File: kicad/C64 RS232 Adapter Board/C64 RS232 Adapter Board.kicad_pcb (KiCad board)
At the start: 2 copper layers, 59.6 x 53.1 mm, 29 parts, among them J1 RS232_HDR, J2 DB25_RS232, J3 C64_USER_PORT, J4 User Port Breakout, SW1 RESET, U1 MAX3241ECAI+T

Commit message: rounded the corner yo
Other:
- board size 59.6 x 53.1 mm -> 60 x 54 mm
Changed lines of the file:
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@@
   (general
     (thickness 1.6)
-    (drawings 37)
+    (drawings 41)
     (tracks 306)
     (zones 0)
@@
     (46 B.CrtYd user)
     (47 F.CrtYd user)
-    (48 B.Fab user hide)
-    (49 F.Fab user hide)
+    (48 B.Fab user)
+    (49 F.Fab user)
   )
   (setup
@@
     (pad_to_mask_clearance 0.05)
     (aux_axis_origin 0 0)
-    (visible_elements 7FFFEFFF)
+    (visible_elements 7FFFF7FF)
     (pcbplotparams
       (layerselection 0x010fc_ffffffff)
@@
     (pad 1 np_thru_hole circle (at 0 0) (size 2.5 2.5) (drill 2.5) (layers *.Cu *.Mask))
   )
-  (gr_line (start 44.196 53.467) (end 103.759 53.467) (layer Edge.Cuts) (width 0.05))
-  (gr_line (start 44.196 106.553) (end 44.196 53.467) (layer Edge.Cuts) (width 0.05))
-  (gr_line (start 103.759 106.553) (end 44.196 106.553) (layer Edge.Cuts) (width 0.05))
-  (gr_line (start 103.759 53.467) (end 103.759 106.553) (layer Edge.Cuts) (width 0.05))
+  (gr_line (start 47 53) (end 101 53) (layer Edge.Cuts) (width 0.05))
+  (gr_line (start 44 104) (end 44 56) (layer Edge.Cuts) (width 0.05))
+  (gr_line (start 101 107) (end 47 107) (layer Edge.Cuts) (width 0.05))
+  (gr_line (start 104 56) (end 104 104) (layer Edge.Cuts) (width 0.05))
+  (gr_arc (start 47 56) (end 47 53) (angle -90) (layer Edge.Cuts) (width 0.05))
+  (gr_arc (start 47 104) (end 44 104) (angle -90) (layer Edge.Cuts) (width 0.05))
+  (gr_arc (start 101 56) (end 104 56) (angle -90) (layer Edge.Cuts) (width 0.05))
+  (gr_arc (start 101 104) (end 101 107) (angle -90) (layer Edge.Cuts) (width 0.05))
   (gr_text PWR (at 89.027 105.41) (layer F.SilkS)
     (effects (font (size 0.5 0.5) (thickness 0.1)))

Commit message: add some labels or something and stuff
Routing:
- net GND: track 5.25 -> 14.3 mm, vias 16 -> 37
- net /DCD_232: track 22.0 -> 18.5 mm, vias 0 -> 2
- net /RI_232: track 25.9 -> 23.9 mm
- net /DTR_232: track 14.4 -> 12.6 mm
- net /RTS_TTL: track 24.0 -> 22.5 mm
- net /DCD_TTL: track 10.1 -> 8.87 mm
- net /TXD_TTL: track 25.4 -> 26.3 mm
- net /RI_TTL: track 13.4 -> 12.7 mm
- net /DTR_TTL: track 24.8 -> 24.3 mm
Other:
- board text added: "5V"
- board text added: "CTS"
- board text added: "DCD"
- board text added: "DSR"
- board text added: "DTR"
- board text added: "RI"
- board text added: "RTS"
- board text added: "RXD"
- board text added: "TXD"

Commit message: let's do that!
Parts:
- added REF**: Bald_Slot_2mm_X_10mm, My Libraries:Bald_Slot_2mm_X_10mm, F.Cu at (72.7, 100.4)
- added REF**: Bald_Slot_2mm_X_10mm, My Libraries:Bald_Slot_2mm_X_10mm, F.Cu at (72.7, 86.9)
- added REF**: Bald_Slot_2mm_X_10mm, My Libraries:Bald_Slot_2mm_X_10mm, F.Cu at (72.7, 73.6)
- added REF**: Bald_Slot_2mm_X_10mm, My Libraries:Bald_Slot_2mm_X_10mm, F.Cu at (72.7, 59.7)
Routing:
- net GND: vias 37 -> 40
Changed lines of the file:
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@@
     (thickness 1.6)
     (drawings 115)
-    (tracks 354)
+    (tracks 357)
     (zones 0)
-    (modules 29)
+    (modules 33)
     (nets 65)
   )
@@
     (via_min_size 0.4)
     (via_min_drill 0.3)
+    (user_via 3 2)
     (uvia_size 0.3)
     (uvia_drill 0.1)
@@
     (add_net "Net-(U1-Pad20)")
     (add_net "Net-(U1-Pad21)")
+  )
+  (module "My Libraries:Bald_Slot_2mm_X_10mm" (layer F.Cu)
+    (at 72.7176 100.4062)
+    (fp_text reference REF** (at 0 0.5) (layer F.SilkS)
+      (effects (font (size 1 1) (thickness 0.15)))
+    )
+    (fp_text value Bald_Slot_2mm_X_10mm (at 0 -0.5) (layer F.Fab)
+      (effects (font (size 1 1) (thickness 0.15)))
+    )
+    (pad 1 thru_hole oval (at 0.0254 -0.0254) (size 4 12) (drill oval 2 10) (layers *.Cu *.Mask))
+  )
+  (module "My Libraries:Bald_Slot_2mm_X_10mm" (layer F.Cu)
+    (at 72.7176 86.8934)
+    (fp_text reference REF** (at 0 0.5) (layer F.SilkS)
+      (effects (font (size 1 1) (thickness 0.15)))
+    )
+    (fp_text value Bald_Slot_2mm_X_10mm (at 0 -0.5) (layer F.Fab)
+      (effects (font (size 1 1) (thickness 0.15)))
+    )
+    (pad 1 thru_hole oval (at 0.0254 -0.0254) (size 4 12) (drill oval 2 10) (layers *.Cu *.Mask))
+  )
+  (module "My Libraries:Bald_Slot_2mm_X_10mm" (layer F.Cu)
+    (at 72.7176 73.5584)
+    (fp_text reference REF** (at 0 0.5) (layer F.SilkS)
+      (effects (font (size 1 1) (thickness 0.15)))
+    )
+    (fp_text value Bald_Slot_2mm_X_10mm (at 0 -0.5) (layer F.Fab)
+      (effects (font (size 1 1) (thickness 0.15)))
+    )
+    (pad 1 thru_hole oval (at 0.0254 -0.0254) (size 4 12) (drill oval 2 10) (layers *.Cu *.Mask))
+  )
+  (module "My Libraries:Bald_Slot_2mm_X_10mm" (layer F.Cu)
+    (at 72.7176 59.7408)
+    (fp_text reference REF** (at 0 0.5) (layer F.SilkS)
+      (effects (font (size 1 1) (thickness 0.15)))
+    )
+    (fp_text value Bald_Slot_2mm_X_10mm (at 0 -0.5) (layer F.Fab)
+      (effects (font (size 1 1) (thickness 0.15)))
+    )
+    (pad 1 thru_hole oval (at 0.0254 -0.0254) (size 4 12) (drill oval 2 10) (layers *.Cu *.Mask))
   )
   (module Package_SO:SSOP-28_5.3x10.2mm_P0.65mm (layer F.Cu)
@@
   (segment (start 98.933 84.963) (end 98.933 81.4832) (width 0.254) (layer B.Cu) (net 6))
   (via (at 98.933 84.963) (size 0.8) (drill 0.4) (layers F.Cu B.Cu) (net 6))
+  (via (at 71.0946 66.675) (size 0.8) (drill 0.4) (layers F.Cu B.Cu) (net 6))
+  (via (at 72.771 66.675) (size 0.8) (drill 0.4) (layers F.Cu B.Cu) (net 6))
+  (via (at 74.2696 66.675) (size 0.8) (drill 0.4) (layers F.Cu B.Cu) (net 6))
   (segment (start 93.894039 91.724303) (end 94.938401 91.724303) (width 0.254) (layer F.Cu) (net 7))
   (segment (start 93.2307 92.387642) (end 93.894039 91.724303) (width 0.254) (layer F.Cu) (net 7))

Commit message: Final Board (maybe?)
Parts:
- removed the REF** at (72.7, 100.4)
- removed the REF** at (72.7, 86.9)
- removed the REF** at (72.7, 73.6)
- removed the REF** at (72.7, 59.7)
- added REF**: 25mil_Hole, My Libraries:25mil_Hole, F.Cu at (71.5, 80.7)
- added e: 25mil_Hole, My Libraries:25mil_Hole, F.Cu at (74.4, 80.7)
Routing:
- net GND: vias 40 -> 37
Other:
- outline, holes or cut-outs redrawn
- board text added: "C64-User Breakout rev1"
- board text added: "RS-232 Breakout rev1"
- board text added: "james@baldengineer.com Hi Chat! You look nice today!"
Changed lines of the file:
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@@
   (general
     (thickness 1.6)
-    (drawings 115)
-    (tracks 357)
+    (drawings 126)
+    (tracks 354)
     (zones 0)
-    (modules 33)
+    (modules 31)
     (nets 65)
   )
   (page A4)
   (layers
-    (0 F.Cu signal)
-    (31 B.Cu signal)
+    (0 F.Cu signal hide)
+    (31 B.Cu signal hide)
     (32 B.Adhes user)
-    (33 F.Adhes user)
+    (33 F.Adhes user hide)
     (34 B.Paste user)
     (35 F.Paste user)
@@
     (add_net "Net-(U1-Pad21)")
   )
-  (module "My Libraries:Bald_Slot_2mm_X_10mm" (layer F.Cu)
-    (at 72.7176 100.4062)
-    (fp_text reference REF** (at 0 0.5) (layer F.SilkS)
-      (effects (font (size 1 1) (thickness 0.15)))
-    )
-    (fp_text value Bald_Slot_2mm_X_10mm (at 0 -0.5) (layer F.Fab)
-      (effects (font (size 1 1) (thickness 0.15)))
-    )
-    (pad 1 thru_hole oval (at 0.0254 -0.0254) (size 4 12) (drill oval 2 10) (layers *.Cu *.Mask))
-  )
-  (module "My Libraries:Bald_Slot_2mm_X_10mm" (layer F.Cu)
-    (at 72.7176 86.8934)
-    (fp_text reference REF** (at 0 0.5) (layer F.SilkS)
-      (effects (font (size 1 1) (thickness 0.15)))
-    )
-    (fp_text value Bald_Slot_2mm_X_10mm (at 0 -0.5) (layer F.Fab)
-      (effects (font (size 1 1) (thickness 0.15)))
-    )
-    (pad 1 thru_hole oval (at 0.0254 -0.0254) (size 4 12) (drill oval 2 10) (layers *.Cu *.Mask))
-  )
-  (module "My Libraries:Bald_Slot_2mm_X_10mm" (layer F.Cu)
-    (at 72.7176 73.5584)
-    (fp_text reference REF** (at 0 0.5) (layer F.SilkS)
-      (effects (font (size 1 1) (thickness 0.15)))
-    )
-    (fp_text value Bald_Slot_2mm_X_10mm (at 0 -0.5) (layer F.Fab)
-      (effects (font (size 1 1) (thickness 0.15)))
-    )
-    (pad 1 thru_hole oval (at 0.0254 -0.0254) (size 4 12) (drill oval 2 10) (layers *.Cu *.Mask))
-  )
-  (module "My Libraries:Bald_Slot_2mm_X_10mm" (layer F.Cu)
-    (at 72.7176 59.7408)
-    (fp_text reference REF** (at 0 0.5) (layer F.SilkS)
-      (effects (font (size 1 1) (thickness 0.15)))
-    )
-    (fp_text value Bald_Slot_2mm_X_10mm (at 0 -0.5) (layer F.Fab)
-      (effects (font (size 1 1) (thickness 0.15)))
-    )
-    (pad 1 thru_hole oval (at 0.0254 -0.0254) (size 4 12) (drill oval 2 10) (layers *.Cu *.Mask))
+  (module "My Libraries:25mil_Hole" (layer F.Cu)
+    (at 74.4474 80.6958)
+    (fp_text reference e (at 0 0.5) (layer F.SilkS) hide
+      (effects (font (size 1 1) (thickness 0.15)))
+    )
+    (fp_text value 25mil_Hole (at 0 -0.5) (layer F.Fab)
+      (effects (font (size 1 1) (thickness 0.15)))
+    )
+    (pad "" np_thru_hole circle (at -0.127 -0.2032) (size 0.635 0.635) (drill 0.635) (layers *.Cu *.Mask))
+  )
+  (module "My Libraries:25mil_Hole" (layer F.Cu)
+    (at 71.4502 80.6958)
+    (fp_text reference REF** (at 0 0.5) (layer F.SilkS) hide
+      (effects (font (size 1 1) (thickness 0.15)))
+    )
+    (fp_text value 25mil_Hole (at 0 -0.5) (layer F.Fab)
+      (effects (font (size 1 1) (thickness 0.15)))
+    )
+    (pad "" np_thru_hole circle (at -0.127 -0.2032) (size 0.635 0.635) (drill 0.635) (layers *.Cu *.Mask))
   )
   (module Package_SO:SSOP-28_5.3x10.2mm_P0.65mm (layer F.Cu)
@@
     (pad 1 np_thru_hole circle (at 0 0) (size 2.5 2.5) (drill 2.5) (layers *.Cu *.Mask))
   )
+  (gr_text "james@baldengineer.com\nHi Chat! You look nice today!" (at 97.028 61.0108) (layer B.SilkS)
+    (effects (font (size 0.8 0.8) (thickness 0.15)) (justify left mirror))
+  )
+  (gr_text "RS-232 Breakout\nrev1" (at 82.0928 56.3626) (layer F.SilkS)
+    (effects (font (size 1 1) (thickness 0.2)) (justify left))
+  )
+  (gr_text "C64-User Breakout\nrev1" (at 68.1482 60.198 270) (layer F.SilkS)
+    (effects (font (size 1 1) (thickness 0.2)) (justify left))
+  )
+  (gr_line (start 101 107) (end 74.9808 107) (layer Edge.Cuts) (width 0.05))
+  (gr_line (start 70.611909 107) (end 47 107) (layer Edge.Cuts) (width 0.05))
+  (gr_line (start 74.9554 53) (end 101 53) (layer Edge.Cuts) (width 0.05))
+  (gr_line (start 47 53) (end 70.5866 53) (layer Edge.Cuts) (width 0.05))
+  (gr_arc (start 72.7964 83.185) (end 74.980799 83.204999) (angle -180.5245759) (layer Edge.Cuts) (width 0.05))
+  (gr_arc (start 72.771 77.8256) (end 70.586601 77.850999) (angle -178.6827396) (layer Edge.Cuts) (width 0.05))
+  (gr_line (start 70.611909 107) (end 70.611909 83.185001) (layer Edge.Cuts) (width 0.05))
+  (gr_line (start 74.9808 107) (end 74.9808 83.205) (layer Edge.Cuts) (width 0.05))
+  (gr_line (start 74.9554 77.851) (end 74.9554 53) (layer Edge.Cuts) (width 0.05))
+  (gr_line (start 70.5866 77.851) (end 70.5866 53) (layer Edge.Cuts) (width 0.05))
   (gr_text GND (at 52.9336 58.2422 90) (layer B.SilkS)
     (effects (font (size 0.6 0.6) (thickness 0.125)) (justify mirror))
@@
     (effects (font (size 0.6 0.6) (thickness 0.125)))
   )
-  (gr_line (start 47 53) (end 101 53) (layer Edge.Cuts) (width 0.05))
   (gr_line (start 44 104) (end 44 56) (layer Edge.Cuts) (width 0.05))
-  (gr_line (start 101 107) (end 47 107) (layer Edge.Cuts) (width 0.05))
   (gr_line (start 104 56) (end 104 104) (layer Edge.Cuts) (width 0.05))
   (gr_arc (start 47 56) (end 47 53) (angle -90) (layer Edge.Cuts) (width 0.05))
@@
   (segment (start 98.933 84.963) (end 98.933 81.4832) (width 0.254) (layer B.Cu) (net 6))
   (via (at 98.933 84.963) (size 0.8) (drill 0.4) (layers F.Cu B.Cu) (net 6))
-  (via (at 71.0946 66.675) (size 0.8) (drill 0.4) (layers F.Cu B.Cu) (net 6))
-  (via (at 72.771 66.675) (size 0.8) (drill 0.4) (layers F.Cu B.Cu) (net 6))
-  (via (at 74.2696 66.675) (size 0.8) (drill 0.4) (layers F.Cu B.Cu) (net 6))
   (segment (start 93.894039 91.724303) (end 94.938401 91.724303) (width 0.254) (layer F.Cu) (net 7))
   (segment (start 93.2307 92.387642) (end 93.894039 91.724303) (width 0.254) (layer F.Cu) (net 7))

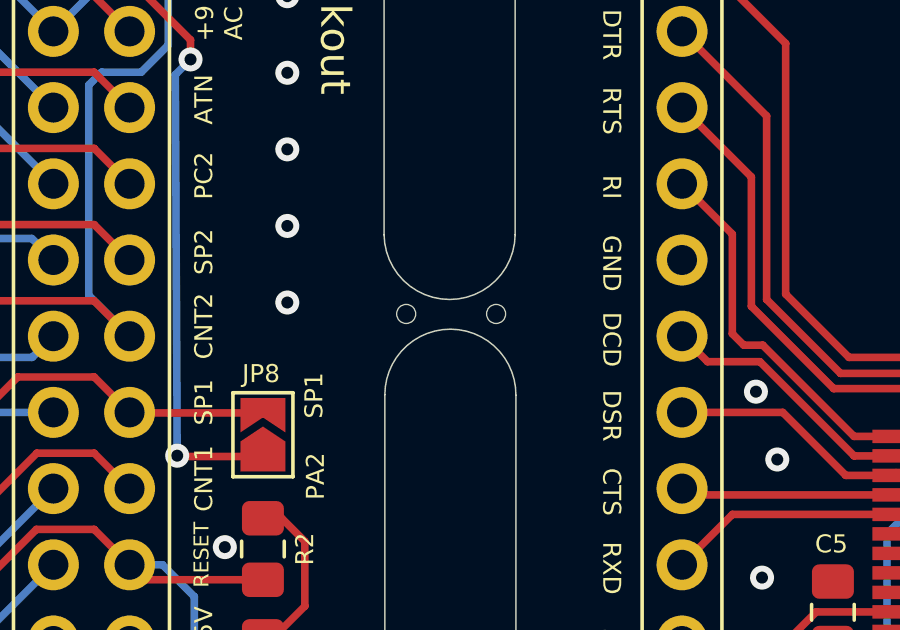
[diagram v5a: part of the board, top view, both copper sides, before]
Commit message: removed 3d files
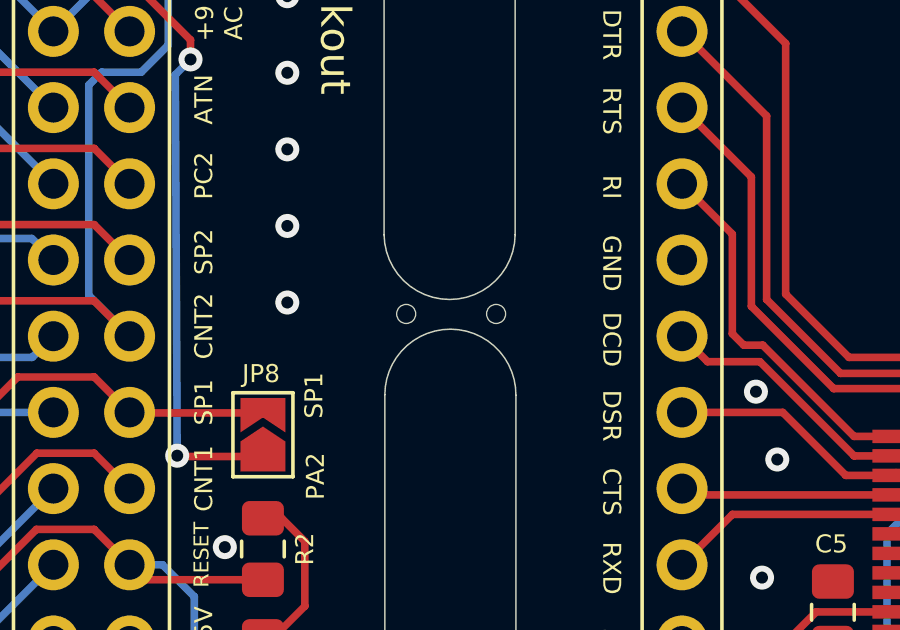
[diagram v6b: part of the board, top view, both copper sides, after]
